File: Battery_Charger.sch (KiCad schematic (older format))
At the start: 44 parts, among them J1 OpenVent_Barrel_Connector, Q10 2N7002BK, Q11 2N7002BK, Q12 2N7002BK, Q8 PBSS5350Z, U13 TLV7042DGKR, U14 BQ24450DW, U16 TLV2333IDR

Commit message: Continuing on with library updates.  Started to fix up the USB interfaces.
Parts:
- D6: Desc (none) -> LED YELLOW/GREEN 1608 SMD; Detailed (none) -> Yellow-Green 572nm LED Indication - Discrete 2.2V 0603 (160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; DistName (none) -> DigiKey; Dist_PN (none) -> SML-D12M8WT86CTR-ND; Mfr (none) -> Rohm Semiconductor
- D7: Detailed (none) -> Diode Standard 1A Surface Mount SMA
- Q10, Q11, Q12: Current (none) -> 350mA; Desc (none) -> MOSFET N-CH 60V 350MA SOT23; Detailed (none) -> N-Channel 350mA (Ta) 370mW (Ta) Surface Mount TO-236AB; DistName (none) -> DigiKey; Dist_PN (none) -> 1727-4789-2-ND; Mfr (none) -> Nexperia USA Inc.; Mfr_PN (none) -> 2N7002BK,215; Voltage (none) -> 60V
- U13: footprint (none) -> Package_SO:VSSOP-8_3.0x3.0mm_P0.65mm; Desc (none) -> IC POWER MANAGEMENT SUPERVISORY; Detailed (none) -> Comparator General Purpose Open-Drain, Rail-to-Rail 8-VSSOP; DistName (none) -> DigiKey; Dist_PN (none) -> 296-TLV7042DGKRTR-ND; Mfr (none) -> Texas Instruments; Mfr_PN (none) -> TLV7042DGKR
- U14: footprint (none) -> Package_SO:SOIC-16W_7.5x12.8mm_P1.27mm; Desc (none) -> IC LEAD ACID CHARGR CTRLR 16SOIC; Detailed (none) -> Charger IC Lead Acid 16-SOIC; DistName (none) -> DigiKey; Dist_PN (none) -> 296-32836-5-ND; Mfr (none) -> Texas Instruments; Mfr_PN (none) -> BQ24450DW
- U16: Desc (none) -> IC OPAMP ZERO-DRIFT 2 CIRC 8SOIC
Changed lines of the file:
@@
 F 1 "2N7002BK" H 5600 4700 50  0000 R BNN
 F 2 "Package_TO_SOT_SMD:SOT-23" H 5050 4600 50  0001 C CNN
-F 3 "" H 5600 4700 50  0001 C CNN
+F 3 "https://assets.nexperia.com/documents/data-sheet/2N7002BK.pdf" H 5600 4700 50  0001 C CNN
+F 4 "350mA" H 5650 5050 50  0001 C CNN "Current"
+F 5 "MOSFET N-CH 60V 350MA SOT23" H 5650 5050 50  0001 C CNN "Desc"
+F 6 "N-Channel 350mA (Ta) 370mW (Ta) Surface Mount TO-236AB" H 5650 5050 50  0001 C CNN "Detailed"
+F 7 "DigiKey" H 5650 5050 50  0001 C CNN "DistName"
+F 8 "1727-4789-2-ND" H 5650 5050 50  0001 C CNN "Dist_PN"
+F 9 "Nexperia USA Inc." H 5650 5050 50  0001 C CNN "Mfr"
+F 10 "2N7002BK,215" H 5650 5050 50  0001 C CNN "Mfr_PN"
+F 11 "60V" H 5650 5050 50  0001 C CNN "Voltage"
 	1    5650 5050
 	-1   0    0    -1
@@
 F 1 "2N7002BK" H 5450 3950 50  0000 R BNN
 F 2 "Package_TO_SOT_SMD:SOT-23" H 4850 3850 50  0001 C CNN
-F 3 "" H 5450 3950 50  0001 C CNN
+F 3 "https://assets.nexperia.com/documents/data-sheet/2N7002BK.pdf" H 5450 3950 50  0001 C CNN
+F 4 "350mA" H 5500 4300 50  0001 C CNN "Current"
+F 5 "MOSFET N-CH 60V 350MA SOT23" H 5500 4300 50  0001 C CNN "Desc"
+F 6 "N-Channel 350mA (Ta) 370mW (Ta) Surface Mount TO-236AB" H 5500 4300 50  0001 C CNN "Detailed"
+F 7 "DigiKey" H 5500 4300 50  0001 C CNN "DistName"
+F 8 "1727-4789-2-ND" H 5500 4300 50  0001 C CNN "Dist_PN"
+F 9 "Nexperia USA Inc." H 5500 4300 50  0001 C CNN "Mfr"
+F 10 "2N7002BK,215" H 5500 4300 50  0001 C CNN "Mfr_PN"
+F 11 "60V" H 5500 4300 50  0001 C CNN "Voltage"
 	1    5500 4300
 	-1   0    0    -1
@@
 F 1 "2N7002BK" H 7800 2550 50  0000 R BNN
 F 2 "Package_TO_SOT_SMD:SOT-23" H 7850 2350 50  0001 C CNN
-F 3 "" H 7800 2550 50  0001 C CNN
+F 3 "https://assets.nexperia.com/documents/data-sheet/2N7002BK.pdf" H 7800 2550 50  0001 C CNN
+F 4 "350mA" H 7850 2900 50  0001 C CNN "Current"
+F 5 "MOSFET N-CH 60V 350MA SOT23" H 7850 2900 50  0001 C CNN "Desc"
+F 6 "N-Channel 350mA (Ta) 370mW (Ta) Surface Mount TO-236AB" H 7850 2900 50  0001 C CNN "Detailed"
+F 7 "DigiKey" H 7850 2900 50  0001 C CNN "DistName"
+F 8 "1727-4789-2-ND" H 7850 2900 50  0001 C CNN "Dist_PN"
+F 9 "Nexperia USA Inc." H 7850 2900 50  0001 C CNN "Mfr"
+F 10 "2N7002BK,215" H 7850 2900 50  0001 C CNN "Mfr_PN"
+F 11 "60V" H 7850 2900 50  0001 C CNN "Voltage"
 	1    7850 2900
 	-1   0    0    -1
@@
 F 9 "S1M-FDITR-ND" H 6900 1050 50  0001 C CNN "Dist_PN"
 F 10 "Diodes Incorporated" H 6900 1050 50  0001 C CNN "Mfr"
+F 11 "Diode Standard 1A Surface Mount SMA" H 6900 1050 50  0001 C CNN "Detailed"
 	1    6900 1050
 	1    0    0    -1
@@
 F 0 "U13" H 2600 6350 50  0000 L CNN
 F 1 "TLV7042DGKR" H 2650 5950 50  0000 L CNN
-F 2 "" H 2100 6050 50  0001 C CNN
-F 3 "" H 2100 6050 50  0001 C CNN
+F 2 "Package_SO:VSSOP-8_3.0x3.0mm_P0.65mm" H 2100 6050 50  0001 C CNN
+F 3 "http://www.ti.com/general/docs/suppproductinfo.tsp?distId=10&gotoUrl=http%3A%2F%2Fwww.ti.com%2Flit%2Fgpn%2Ftlv7042" H 2100 6050 50  0001 C CNN
+F 4 "IC POWER MANAGEMENT SUPERVISORY" H 2100 6050 50  0001 C CNN "Desc"
+F 5 "Comparator General Purpose Open-Drain, Rail-to-Rail 8-VSSOP" H 2100 6050 50  0001 C CNN "Detailed"
+F 6 "DigiKey" H 2100 6050 50  0001 C CNN "DistName"
+F 7 "296-TLV7042DGKRTR-ND" H 2100 6050 50  0001 C CNN "Dist_PN"
+F 8 "Texas Instruments" H 2100 6050 50  0001 C CNN "Mfr"
+F 9 "TLV7042DGKR" H 2100 6050 50  0001 C CNN "Mfr_PN"
 	1    2100 6050
 	1    0    0    -1
@@
 F 0 "U13" H 5050 7217 50  0000 C CNN
 F 1 "TLV7042DGKR" H 5050 7126 50  0000 C CNN
-F 2 "" H 4650 6750 50  0001 C CNN
-F 3 "" H 4650 6750 50  0001 C CNN
+F 2 "Package_SO:VSSOP-8_3.0x3.0mm_P0.65mm" H 4650 6750 50  0001 C CNN
+F 3 "http://www.ti.com/general/docs/suppproductinfo.tsp?distId=10&gotoUrl=http%3A%2F%2Fwww.ti.com%2Flit%2Fgpn%2Ftlv7042" H 4650 6750 50  0001 C CNN
+F 4 "IC POWER MANAGEMENT SUPERVISORY" H 4650 6750 50  0001 C CNN "Desc"
+F 5 "Comparator General Purpose Open-Drain, Rail-to-Rail 8-VSSOP" H 4650 6750 50  0001 C CNN "Detailed"
+F 6 "DigiKey" H 4650 6750 50  0001 C CNN "DistName"
+F 7 "296-TLV7042DGKRTR-ND" H 4650 6750 50  0001 C CNN "Dist_PN"
+F 8 "Texas Instruments" H 4650 6750 50  0001 C CNN "Mfr"
+F 9 "TLV7042DGKR" H 4650 6750 50  0001 C CNN "Mfr_PN"
 	2    4650 6750
 	1    0    0    -1
@@
 F 1 "LED_GREEN_0603_SMD" H 1650 4100 60  0001 C CNN
 F 2 "LED_SMD:LED_0603_1608Metric" H 1650 4100 50  0001 C CNN
-F 3 "" H 1650 4100 50  0001 C CNN
+F 3 "https://www.rohm.com/datasheet/SML-D12M8W(C)/sml-d12x8(c)-e" H 1650 4100 50  0001 C CNN
 F 4 "SML-D12M8WT86C" V 1650 4100 50  0001 C CNN "Mfr_PN"
 F 5 "" V 1995 4230 50  0000 L CNN "Val"
 F 6 "GREEN" H 1650 4100 50  0001 C CNN "Colour"
+F 7 "LED YELLOW/GREEN 1608 SMD" H 1650 4100 50  0001 C CNN "Desc"
+F 8 "Yellow-Green 572nm LED Indication - Discrete 2.2V 0603 (1608 Metric)" H 1650 4100 50  0001 C CNN "Detailed"
+F 9 "DigiKey" H 1650 4100 50  0001 C CNN "DistName"
+F 10 "SML-D12M8WT86CTR-ND" H 1650 4100 50  0001 C CNN "Dist_PN"
+F 11 "Rohm Semiconductor" H 1650 4100 50  0001 C CNN "Mfr"
 	1    1650 4100
 	0    1    1    0
@@
 F 0 "U14" H 5100 1150 50  0000 C CNN
 F 1 "BQ24450DW" H 5150 1000 50  0000 C CNN
-F 2 "" H 4150 1650 50  0001 C CNN
-F 3 "" H 4150 1650 50  0001 C CNN
+F 2 "Package_SO:SOIC-16W_7.5x12.8mm_P1.27mm" H 4150 1650 50  0001 C CNN
+F 3 "http://www.ti.com/general/docs/suppproductinfo.tsp?distId=10&gotoUrl=http%3A%2F%2Fwww.ti.com%2Flit%2Fgpn%2Fbq24450" H 4150 1650 50  0001 C CNN
+F 4 "IC LEAD ACID CHARGR CTRLR 16SOIC" H 4150 1650 50  0001 C CNN "Desc"
+F 5 "Charger IC Lead Acid 16-SOIC" H 4150 1650 50  0001 C CNN "Detailed"
+F 6 "DigiKey" H 4150 1650 50  0001 C CNN "DistName"
+F 7 "296-32836-5-ND" H 4150 1650 50  0001 C CNN "Dist_PN"
+F 8 "Texas Instruments" H 4150 1650 50  0001 C CNN "Mfr"
+F 9 "BQ24450DW" H 4150 1650 50  0001 C CNN "Mfr_PN"
 	1    4150 1650
 	1    0    0    -1
@@
 F 7 "296-43772-2-ND" H 8600 2450 50  0001 C CNN "Dist_PN"
 F 8 "Zero-Drift Amplifier Circuit Rail-to-Rail 8-SOIC" H 8600 2450 50  0001 C CNN "Detailed"
+F 9 "IC OPAMP ZERO-DRIFT 2 CIRC 8SOIC" H 8600 2450 50  0001 C CNN "Desc"
 	1    8600 2450
 	1    0    0    -1
@@
 F 7 "296-43772-2-ND" H 9700 3600 50  0001 C CNN "Dist_PN"
 F 8 "Zero-Drift Amplifier Circuit Rail-to-Rail 8-SOIC" H 9700 3600 50  0001 C CNN "Detailed"
+F 9 "IC OPAMP ZERO-DRIFT 2 CIRC 8SOIC" H 9700 3600 50  0001 C CNN "Desc"
 	2    9700 3600
 	1    0    0    -1

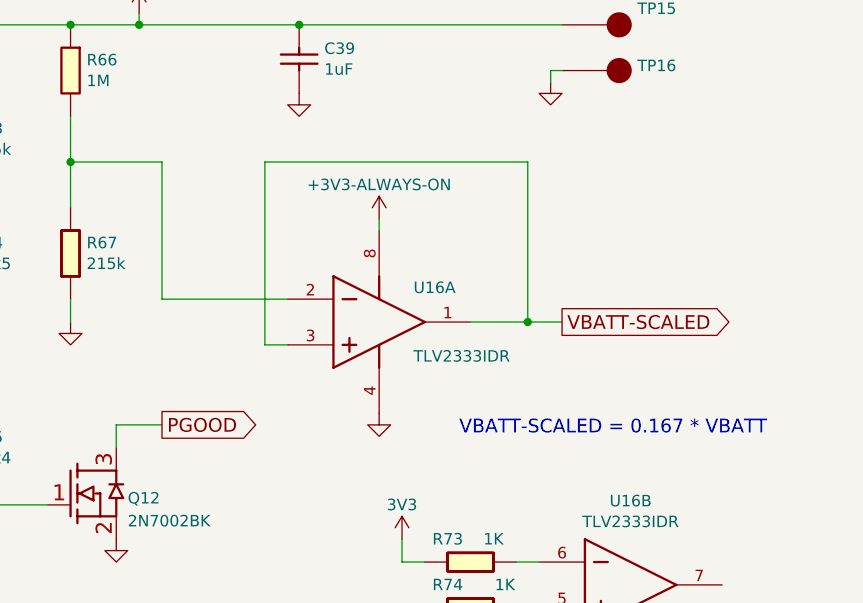
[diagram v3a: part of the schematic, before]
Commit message: Tweaked some issues on the battery charger page.
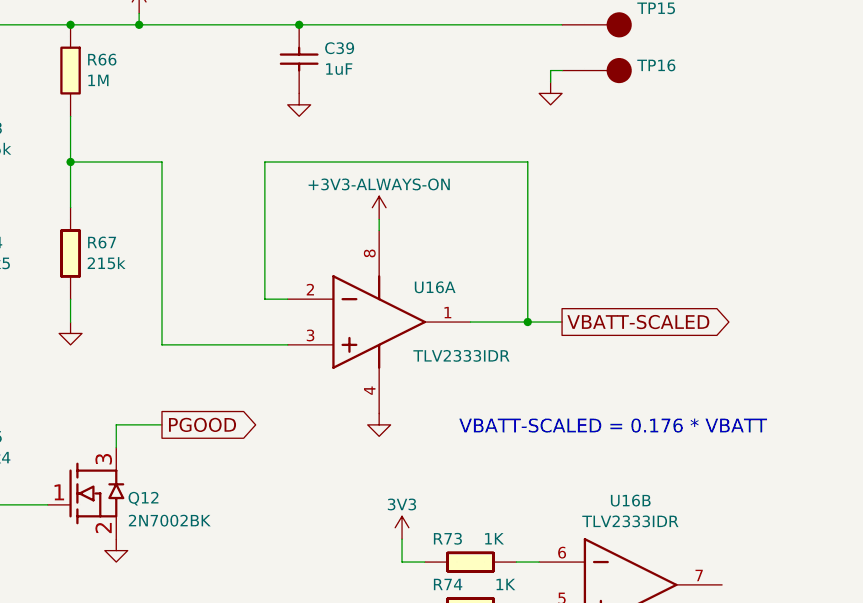
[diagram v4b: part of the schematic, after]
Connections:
- net VBATT-SCALED: now also U16.2 (INA-); no longer U16.3 (INA+)
- net at R66.2, R67.1: now also U16.3 (INA+); no longer U16.2 (INA-)
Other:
- note added: "VBATT-SCALED = 0.176 * VBATT"
- note removed: "VBATT-SCALED = 0.167 * VBATT"
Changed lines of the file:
@@
 VDC Alert set to 10V
 Text Notes 9350 2850 0    60   ~ 0
-VBATT-SCALED = 0.167 * VBATT
+VBATT-SCALED = 0.176 * VBATT
 Text GLabel 3200 2450 0    60   Output ~ 0
 ISNS
@@
 	6650 1750 6650 1850
 Wire Wire Line
-	8050 2250 8600 2250
-Wire Wire Line
-	8050 1650 8050 2250
-Wire Wire Line
 	7650 1650 8050 1650
 Wire Wire Line
@@
 Wire Wire Line
 	8500 1650 9650 1650
-Wire Wire Line
-	8500 2450 8500 1650
-Wire Wire Line
-	8600 2450 8500 2450
 Wire Wire Line
 	1800 6050 1800 5750
@@
 Wire Wire Line
 	4050 6750 4050 6800
+Wire Wire Line
+	8600 2250 8500 2250
+Wire Wire Line
+	8500 2250 8500 1650
+Wire Wire Line
+	8050 1650 8050 2450
+Wire Wire Line
+	8050 2450 8600 2450
 $EndSCHEMATC

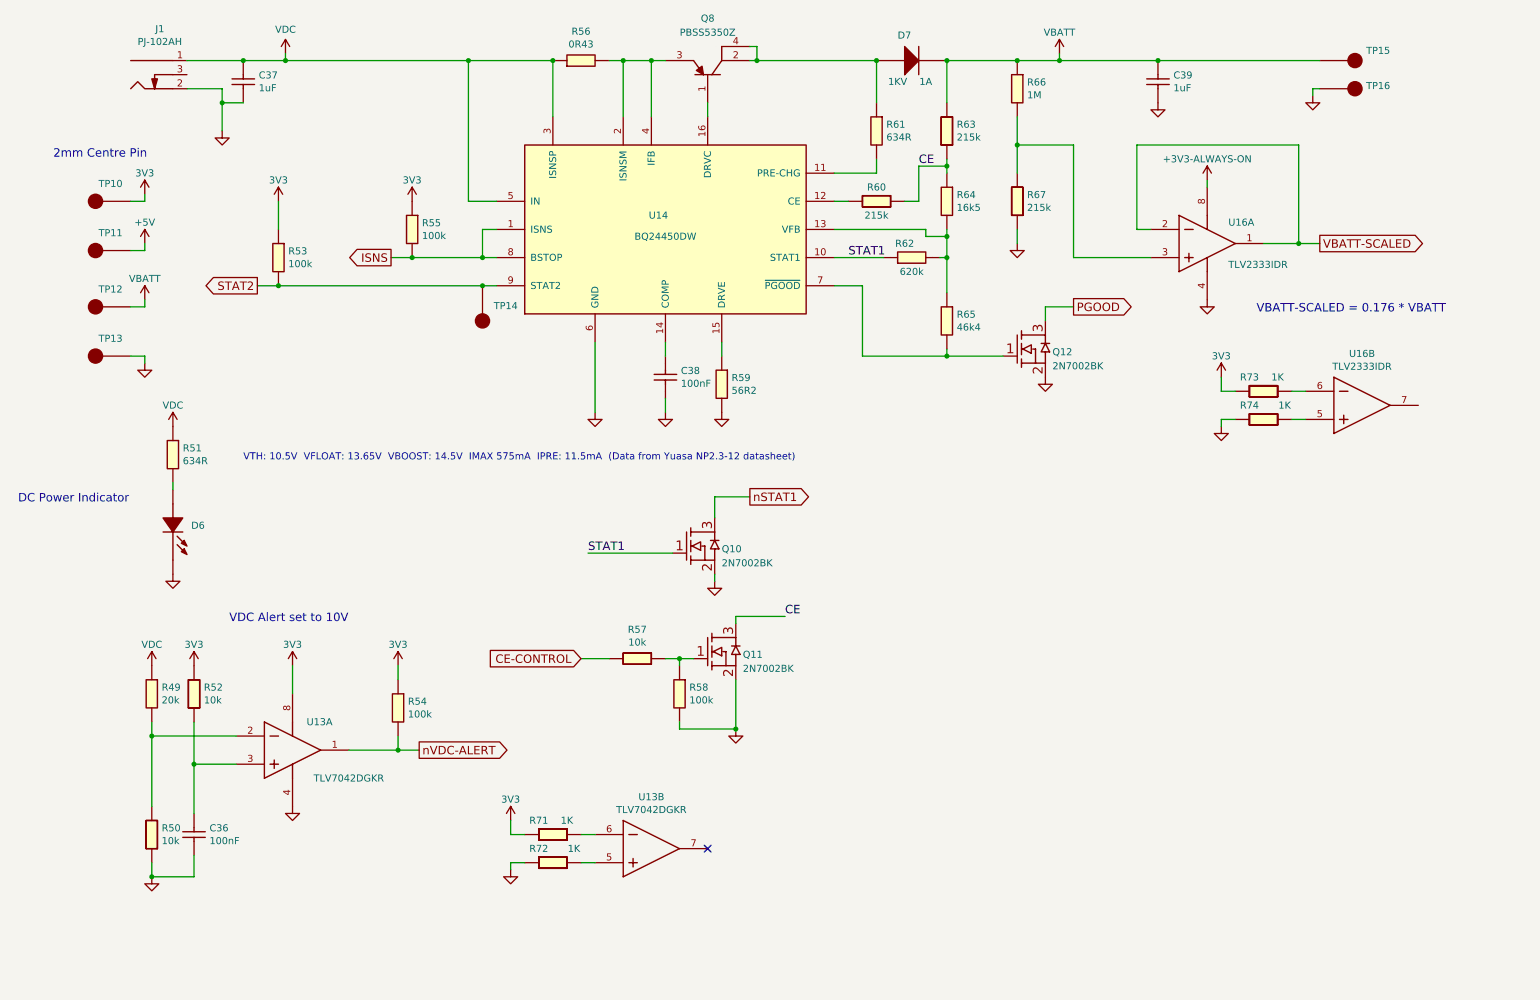
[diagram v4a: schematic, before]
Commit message: Battery Charger page mostly finished, might want to think about what to do with the battery charging current signal (it's analog).
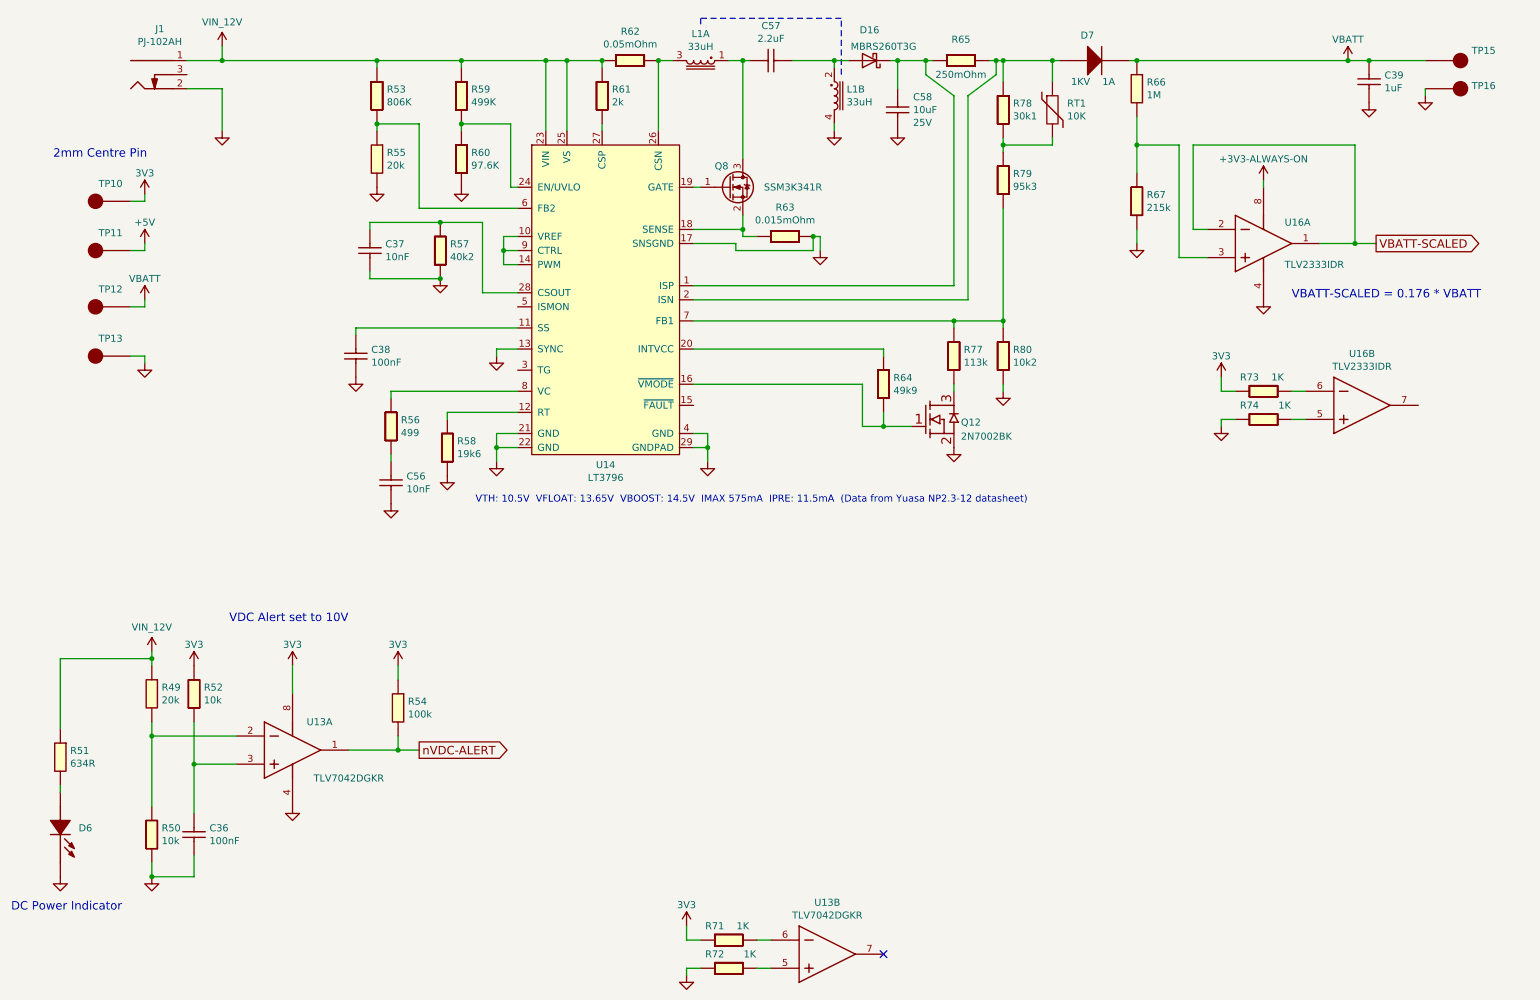
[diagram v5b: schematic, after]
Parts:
- removed C37: 1uF_0603_Ceramic_Capacitor,_10%,_50V,_X5R, Capacitor_SMD:C_0603_1608Metric, symbol OpenVent:1uF_0603_Ceramic_Capacitor,_10%,_50V,_X5R
- removed Q10, Q11: 2N7002BK, Package_TO_SOT_SMD:SOT-23, symbol OpenVent:2N7002BK
- removed Q8: PBSS5350Z, Package_TO_SOT_SMD:SOT-223, symbol OpenVent:PBSS5350Z
- removed R53, R55, R58: 100K_0603_Chip_Resistor,_1%,_0.1W, Resistor_SMD:R_0603_1608Metric, symbol OpenVent:100K_0603_Chip_Resistor,_1%,_0.1W
- removed R56: 0R43_1210_Chip_Resistor,_1%,_0.5W, Resistor_SMD:R_1210_3225Metric, symbol OpenVent:0R43_1210_Chip_Resistor,_1%,_0.5W
- removed R57: 10k_0603_Chip_Resistor,_1%,_0.1W, Resistor_SMD:R_0603_1608Metric, symbol OpenVent:10k_0603_Chip_Resistor,_1%,_0.1W
- removed R59: 562R_0603_Chip_Resistor,_1%,_0.1W, Resistor_SMD:R_0603_1608Metric, symbol OpenVent:562R_0603_Chip_Resistor,_1%,_0.1W
- removed R60, R63: 215k_0603_Chip_Resistor,_1%,_0.1W, Resistor_SMD:R_0603_1608Metric, symbol OpenVent:215k_0603_Chip_Resistor,_1%,_0.1W
- removed R61: 634R_0603_Chip_Resistor,_1%,_0.1W, Resistor_SMD:R_0603_1608Metric, symbol OpenVent:634R_0603_Chip_Resistor,_1%,_0.1W
- removed R62: 620k_0603_Chip_Resistor,_1%,_0.1W, Resistor_SMD:R_0603_1608Metric, symbol OpenVent:620k_0603_Chip_Resistor,_1%,_0.1W
- removed R64: 16k5_0603_Chip_Resistor,_1%,_0.1W, Resistor_SMD:R_0603_1608Metric, symbol OpenVent:16k5_0603_Chip_Resistor,_1%,_0.1W
- removed R65: 46k4_0603_Chip_Resistor,_1%,_0.1W, Resistor_SMD:R_0603_1608Metric, symbol OpenVent:46k4_0603_Chip_Resistor,_1%,_0.1W
- removed TP14: Test_Point_PTH, TestPoint:TestPoint_Pad_2.0x2.0mm, symbol OpenVent:Test_Point_PTH
- removed U14: BQ24450DW, Package_SO:SOIC-16W_7.5x12.8mm_P1.27mm, symbol OpenVent:BQ24450DW
- added C37, C56: 10nF_0603_Ceramic_Capacitor,_10%,_50V,_X7R-, symbol OpenVent:10nF_0603_Ceramic_Capacitor,_10%,_50V,_X7R-
- added C57: 2.2uF_2824_film_capacitor_10%_40V, symbol OpenVent:2.2uF_2824_film_capacitor_10%_40V
- added C58: C_1210_10uF_25V_10%_X7R, Capacitor_SMD:C_1210_3225Metric, symbol OpenVent:C_1210_10uF_25V_10%_X7R
- added D16: MBRS260T3G, Diode_SMD:D_SMB, symbol OpenVent:MBRS260T3G
- added L1: MSD1260-333, F_Inductors:MSD1260, symbol F_inductors:MSD1260-333
- added Q8: SSM3K341R, Package_TO_SOT_SMD:SOT-23, symbol OpenVent:SSM3K341R
- added R53: R_0603_806K_0.1W_1%, symbol OpenVent:R_0603_806K_0.1W_1%
- added R55: 20k_0603_Chip_Resistor,_1%,_0.1W, symbol OpenVent:20k_0603_Chip_Resistor,_1%,_0.1W
- added R56: R_0603_499R_0.1W_1%, symbol OpenVent:R_0603_499R_0.1W_1%
- added R57: R_0603_40k2K_0.1W_1%, symbol OpenVent:R_0603_40k2K_0.1W_1%
- added R58: R_0603_19k6_0.1W_1%, symbol OpenVent:R_0603_19k6_0.1W_1%
- added R59: R_0603_499K_0.1W_1%, symbol OpenVent:R_0603_499K_0.1W_1%
- added R60: R_0603_97.6K_0.1W_1%, symbol OpenVent:R_0603_97.6K_0.1W_1%
- added R61: R_0603_2k_0.1W_1%, symbol OpenVent:R_0603_2k_0.1W_1%
- added R62: R_0805_050m_cursense, Resistor_SMD:R_0805_2012Metric, symbol OpenVent:R_0805_050m_cursense
- added R63: R_0603_015m_cursense, Resistor_SMD:R_0603_1608Metric, symbol OpenVent:R_0603_015m_cursense
- added R64: R_0603_49k9_0.1W_1%, symbol OpenVent:R_0603_49k9_0.1W_1%
- added R65: R_1206_250m_cursense, Resistor_SMD:R_1206_3216Metric, symbol OpenVent:R_1206_250m_cursense
- added R77: R_0603_113k_0.1W_1%, symbol OpenVent:R_0603_113k_0.1W_1%
- added R78: R_0603_30k1_0.1W_1%, symbol OpenVent:R_0603_30k1_0.1W_1%
- added R79: R_0603_95k3_0.1W_1%, symbol OpenVent:R_0603_95k3_0.1W_1%
- added R80: R_0603_10k2_0.1W_1%, symbol OpenVent:R_0603_10k2_0.1W_1%
- added RT1: R_Thermistor_0603_10K_NTC, Resistor_SMD:R_0603_1608Metric, symbol OpenVent:R_Thermistor_0603_10K_NTC
- added U14: LT3796, F_ICs:TSSOP-28-LTvar_EB_4.4x9.7mm_P0.65mm, symbol F_ICs:LT3796
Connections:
- net GND: now also C37.2, C56.2, C58.2, L1.4, R55.2, R57.2, R58.2, R60.2, R63.1, R80.2, U14.13 (SYNC), U14.17 (SNSGND), U14.21 (GND), U14.22 (GND), U14.29 (GNDPAD), U14.4 (GND)
- net VDC: no longer J1.1 (Centre), R49.1, R51.1
- net at D7.1 (A): now also R65.2, R78.1, RT1.1, U14.2 (ISN)
- net at Q12.1 (G1): now also R64.2, U14.16 (~VMODE~)
- net at C38.1: now also U14.11 (SS)
- net PGOOD: no longer names the net of Q12.3 (D)
- net PGOOD: now also R77.2
- new net: C58.1, D16.1 (K), R65.1, U14.1 (ISP)
- new net: C57.2, D16.2 (A), L1.2
- new net: U14.10 (VREF), U14.14 (PWM), U14.9 (CTRL)
- new net: R58.1, U14.12 (RT)
- new net: Q8.2 (S), R63.2, U14.18 (SENSE)
- new net: Q8.1 (G), U14.19 (GATE)
- new net: R64.1, U14.20 (INTVCC)
- new net: R59.2, R60.1, U14.24 (EN/UVLO)
- new net: L1.3 (4), R62.2, U14.26 (CSN)
- new net: R61.2, U14.27 (CSP)
- new net: C37.1, R57.1, U14.28 (CSOUT)
- new net: R53.2, R55.1, U14.6 (FB2)
- new net: R77.1, R79.2, R80.1, U14.7 (FB1)
- new net: R56.1, U14.8 (VC)
- new net: C57.1, L1.1 (2), Q8.3 (D)
- new net: R78.2, R79.1, RT1.2
- new net: C56.1, R56.2
- new net VIN: J1.1 (Centre), R49.1, R51.1, R53.1, R59.1, R61.1, R62.1, U14.23 (VIN), U14.25 (VS)
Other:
- moved on the sheet: C38, C39, D6, D7, Q12, R51, R66, R67, R71, R72, TP15, TP16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
